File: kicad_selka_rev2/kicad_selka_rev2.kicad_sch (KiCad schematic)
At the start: 88 parts, among them J1 Conn_01x02, J2 Conn_01x06, J3 Conn_01x08, J4 Conn_01x08, SW1 PUSH, U1 ATtiny861A SOIC20

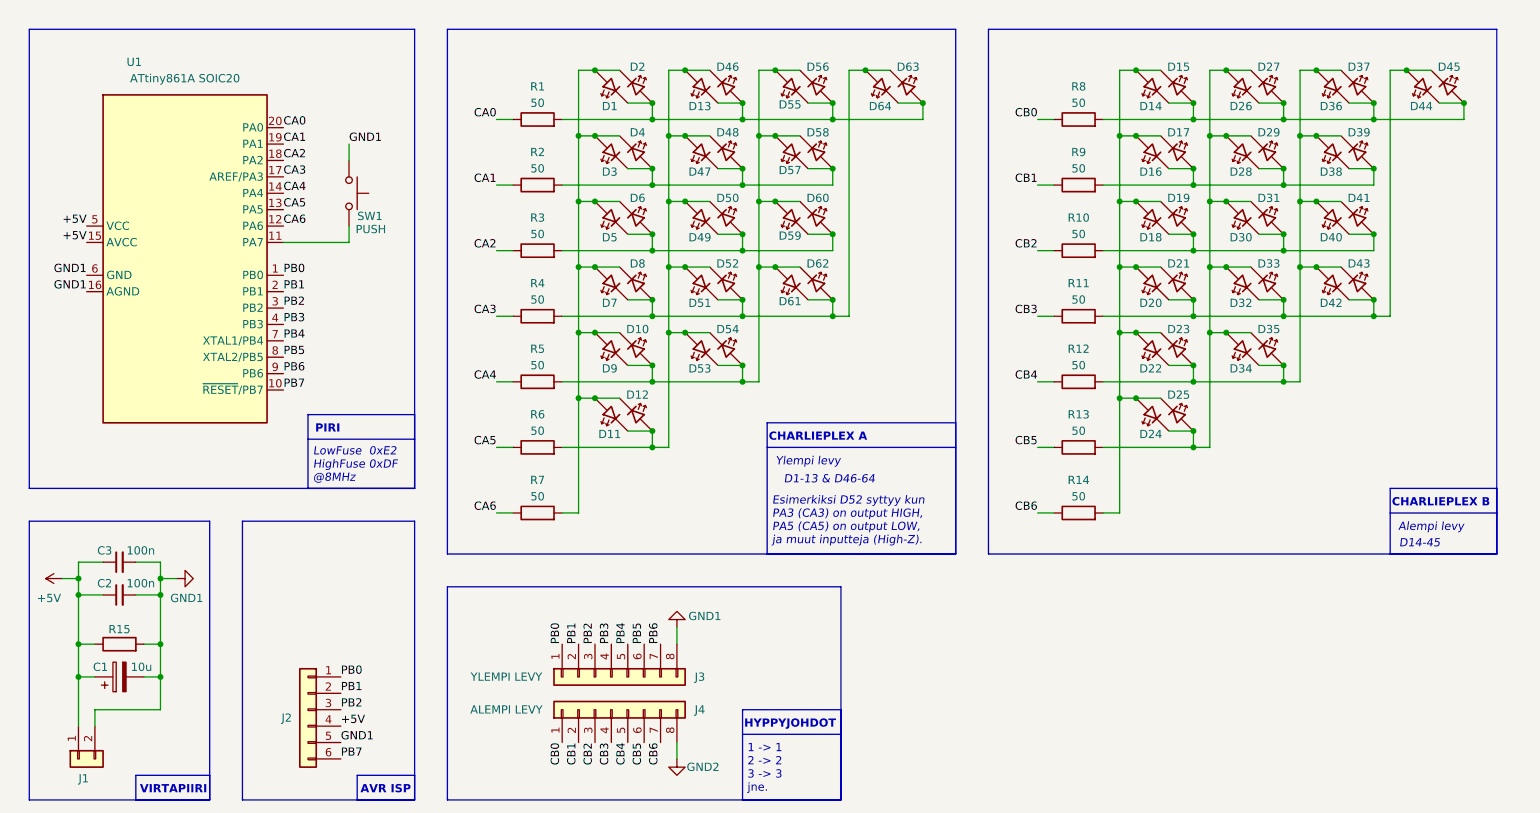
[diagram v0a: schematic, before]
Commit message: Selkäsalama rev2 done
Skema ja leiska valmis rev2.
Tilattu R2-260625. Toimii ja näyttää hjuvalta.

Siirtin kamaa /archive kansioon. mm. vanhat ja proto versiot.
Vanhat media tiedostot jne.
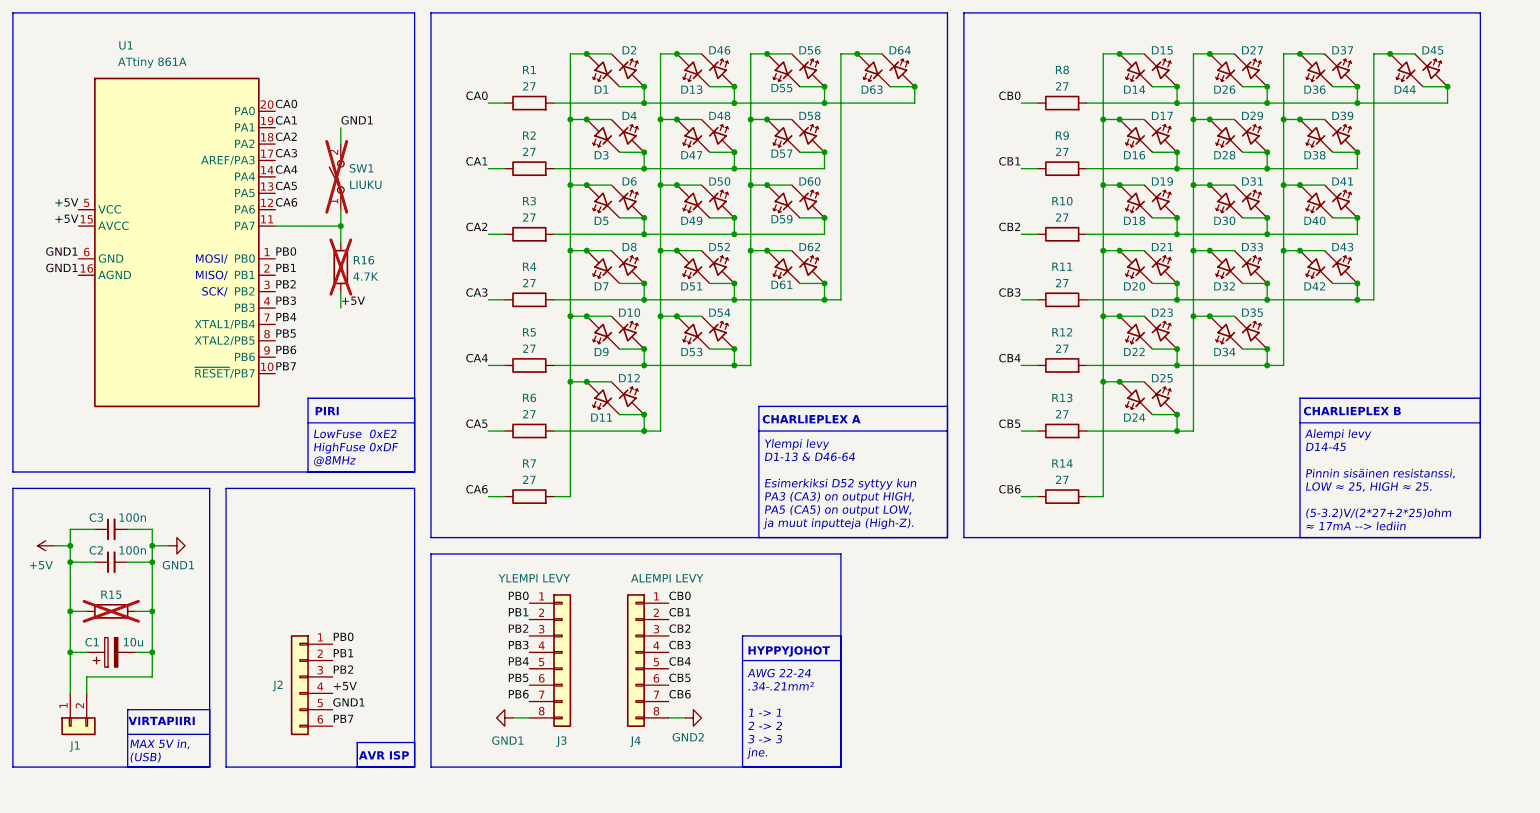
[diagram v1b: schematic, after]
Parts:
- removed SW1: PUSH, Connector_PinHeader_2.00mm:PinHeader_1x02_P2.00mm_Vertical, symbol Switch:SW_Push
- added R16: 4.7K, Resistor_SMD:R_0805_2012Metric_Pad1.20x1.40mm_HandSolder, symbol Device:R
- added SW1: LIUKU, Connector_PinHeader_2.54mm:PinHeader_1x02_P2.54mm_Vertical, symbol Switch:SW_SPST
- C2, C3: footprint Capacitor_SMD:C_0805_2012Metric_Pad1.18x1.45mm_HandSolder -> Capacitor_SMD:C_1206_3216Metric_Pad1.33x1.80mm_HandSolder
- D1, D10, D11, D12, D13, D14, D15, D16, D17, D18, D19, D2, D20, D21, D22, D23, D24, D25, D26, D27, D28, D29, D3, D30, D31, D32, D33, D34, D35, D36, D37, D38, D39, D4, D40, D41, D42, D43, D44, D45, D46, D47, D48, D49, D5, D50, D51, D52, D53, D54, D55, D56, D57, D58, D59, D6, D60, D61, D62, D7, D8, D9: footprint (none) -> footprintteja:LED_D5.0mm_blue_zani
- D63: renamed from D64; footprint (none) -> footprintteja:LED_D5.0mm_blue_zani
- D64: renamed from D63; footprint (none) -> footprintteja:LED_D5.0mm_blue_zani
- J2: footprint footprintteja:PinHeader_1x06_P2.00mm_Horizontal_smd_tht -> footprintteja:PinHeader_1x06_P2.54mm_Horizontal_smd_tht
- R1, R10, R11, R12, R13, R14, R2, R3, R4, R5, R6, R7, R8, R9: value 50 -> 27; footprint Resistor_SMD:R_1210_3225Metric_Pad1.30x2.65mm_HandSolder -> Resistor_SMD:R_1206_3216Metric_Pad1.30x1.75mm_HandSolder
- R15: now not fitted
- U1: value ATtiny861A SOIC20 -> ATtiny 861A
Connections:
- net +5V: now also R16.1
- net GND1: now also SW1.2 (B)
- net at U1.11 (PA7): now also R16.2, SW1.1 (A)
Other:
- note added: "AWG 22-24 .34-.21mm² 1 -> 1 2 -> 2 3 -> 3 jne."
- note added: "Alempi levy D14-45 Pinnin sisäinen resistanssi, LOW ≈ 25, HIGH ≈ 25. (5-3.2)V/(2*27+2*25)ohm ≈ 17mA --> lediin"
- note added: "HYPPYJOHOT"
- note added: "MAX 5V in, (USB)"
- note added: "MISO/"
- note added: "MOSI/"
- note added: "SCK/"
- note added: "Ylempi levy D1-13 & D46-64 Esimerkiksi D52 syttyy kun PA3 (CA3) on output HIGH, PA5 (CA5) on output LOW, ja muut inputteja (High-Z)."
- note removed: "1 -> 1 2 -> 2 3 -> 3 jne."
- note removed: "Alempi levy"
- note removed: "D1-13 & D46-64"
- note removed: "D14-45"
- note removed: "Esimerkiksi D52 syttyy kun PA3 (CA3) on output HIGH, PA5 (CA5) on output LOW, ja muut inputteja (High-Z)."
- note removed: "HYPPYJOHDOT"
- note removed: "Ylempi levy"
- moved on the sheet: C1, C2, C3, D1, D10, D11, D12, D13, D14, D15, D16, D17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
